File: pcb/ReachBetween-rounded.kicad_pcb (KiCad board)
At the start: 2 copper layers, 51.8 x 73.5 mm, 11 parts, among them J1 IN, J2 Out A, J3 Out B

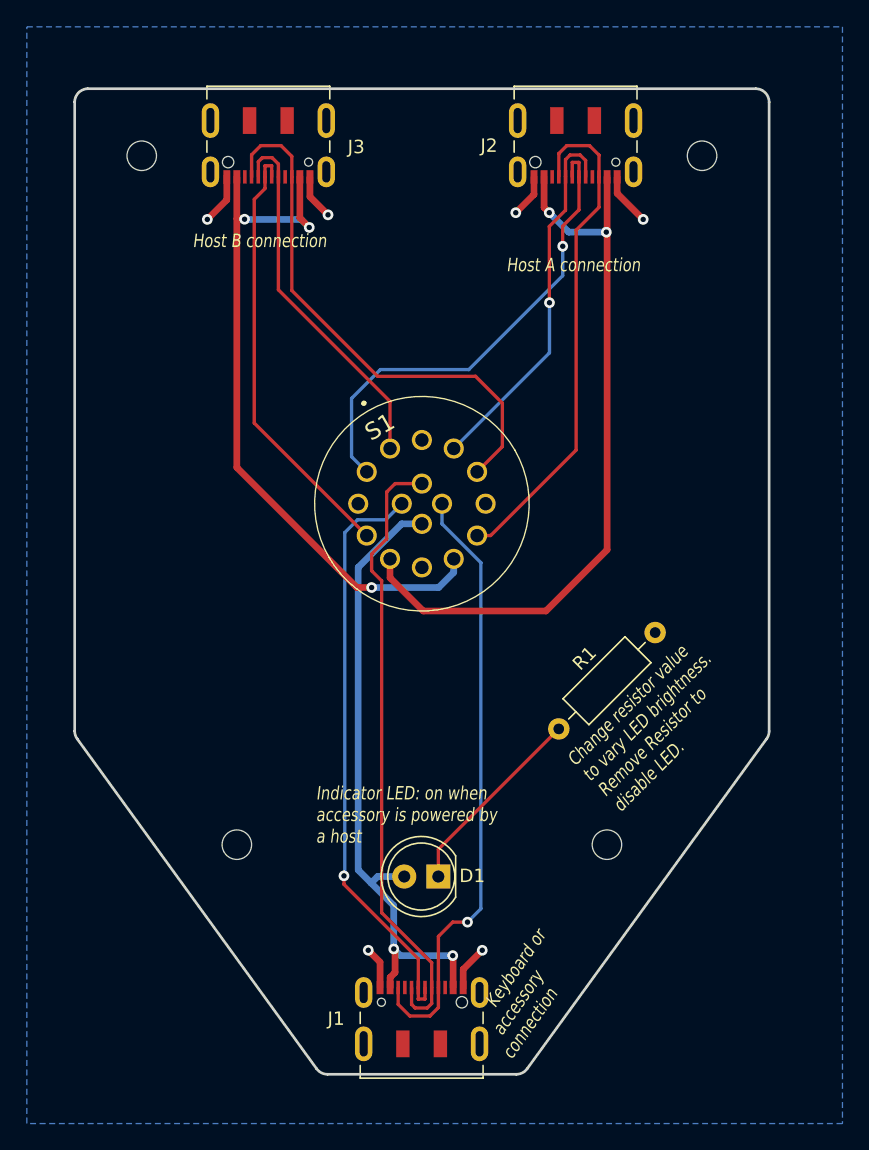
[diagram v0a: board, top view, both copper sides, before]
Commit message: Round tracks
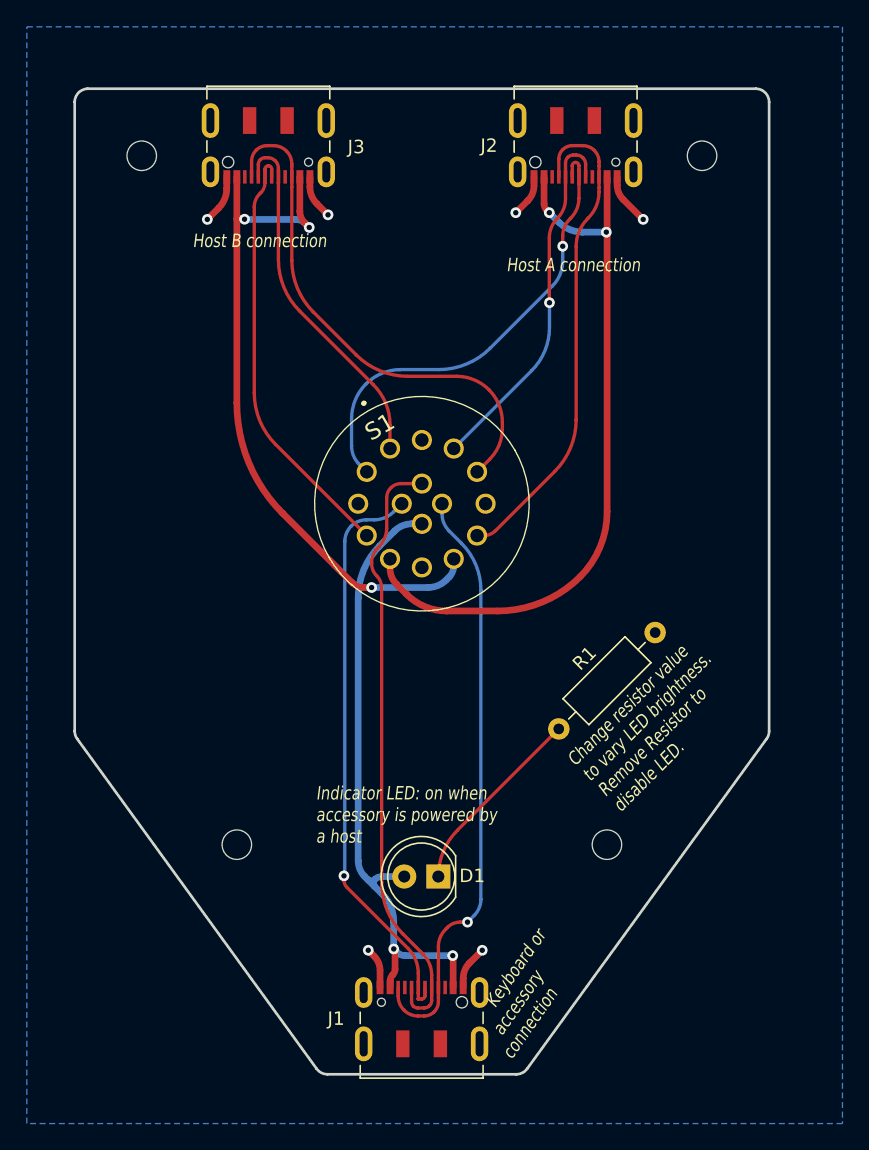
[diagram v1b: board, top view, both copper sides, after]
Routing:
- net /D+ A: track 36.0 -> 34.8 mm
- net /CC B: track 40.3 -> 39.1 mm
- net /VBUS A: track 56.0 -> 54.8 mm
- net /VBUS B: track 52.8 -> 51.9 mm
- net /D- in: track 46.4 -> 45.5 mm
- net /CC A: track 38.0 -> 37.2 mm
- net /CC in: track 45.6 -> 44.8 mm
- net /D+ B: track 32.7 -> 32.1 mm
- net /D- B: track 27.6 -> 27.0 mm
- net /D- A: track 28.0 -> 27.5 mm
- net /D+ in: track 43.6 -> 43.1 mm

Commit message: Teardrop tracks
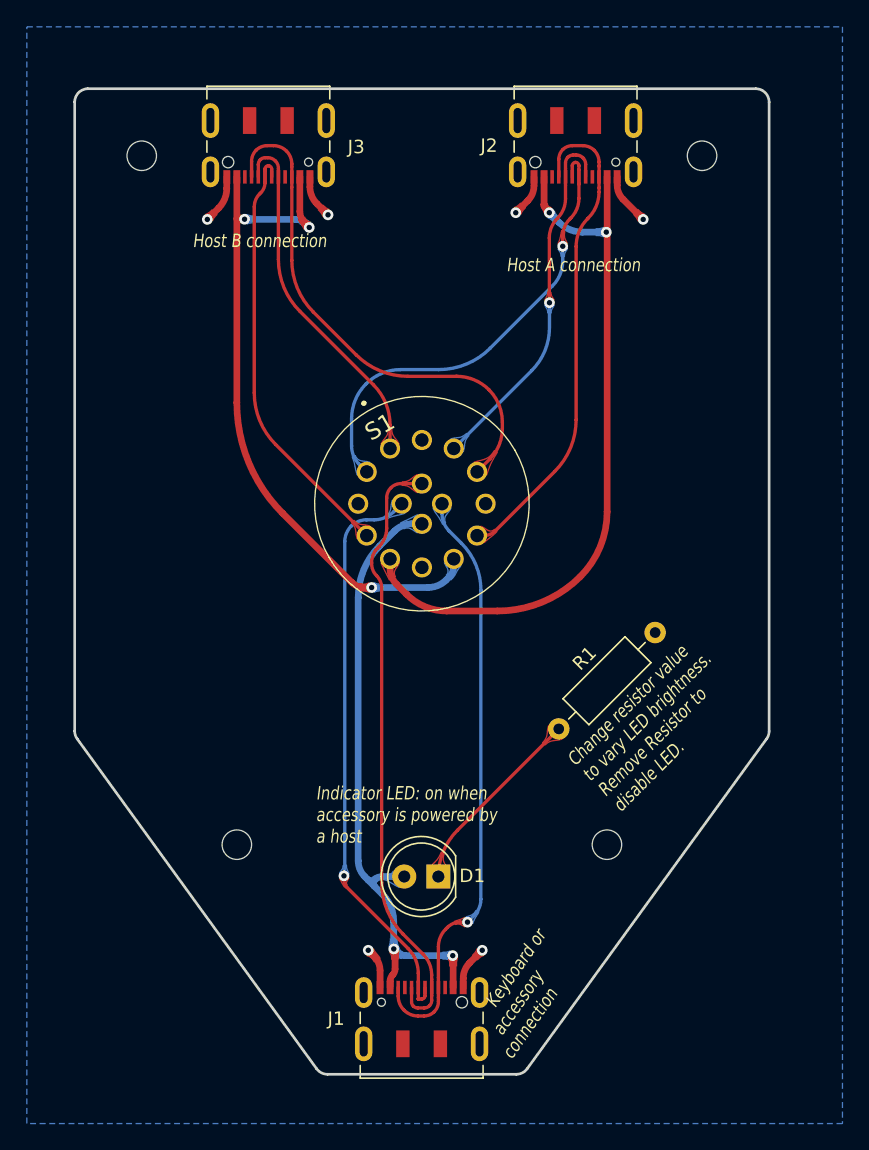
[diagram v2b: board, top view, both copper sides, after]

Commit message: Update version number
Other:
- board text added: "RB02 v1.1.2 © Will Harris-Braun 2022-04-17"
- board text removed: "RB02 v1.1.0 © Will Harris-Braun 2022-04-17"
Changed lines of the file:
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@@
     (effects (font (size 1.5 1.3) (thickness 0.3)) (justify mirror))
   )
-  (gr_text "RB02 v1.1.0\n© Will Harris-Braun\n2022-04-17" (at 142.5 94.2) (layer "B.SilkS")
+  (gr_text "RB02 v1.1.2\n© Will Harris-Braun\n2022-04-17" (at 142.5 94.2) (layer "B.SilkS")
     (effects (font (size 1 0.8) (thickness 0.1)) (justify left mirror))
   )

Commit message: Round silkscreen lines on back
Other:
- board text added: "RB02 v1.1.3 © Will Harris-Braun 2022-04-17"
- board text removed: "RB02 v1.1.2 © Will Harris-Braun 2022-04-17"
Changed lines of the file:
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@@
     ) (layer "B.SilkS") (width 0.025) (fill solid))
   (gr_rect (start 151 117.7) (end 149 119.7) (layer "B.SilkS") (width 0) (fill solid))
-  (gr_line (start 143.75 89.7) (end 138.5 85.7) (layer "B.SilkS") (width 2))
   (gr_poly
     (pts
@@
   (gr_rect (start 149 126.2) (end 151 124.2) (layer "B.SilkS") (width 0) (fill solid))
   (gr_line (start 150 101.8) (end 150 118.7) (layer "B.SilkS") (width 2))
+  (gr_arc (start 161.6 80.9) (mid 160.542149 85.3677) (end 157.55 88.85) (layer "B.SilkS") (width 2))
+  (gr_poly
+    (pts
+      (xy 143.401315 88.331702)
+      (xy 144.962176 89.582187)
+      (xy 143.711691 91.143048)
+      (xy 142.15083 89.892563)
+    ) (layer "B.SilkS") (width 0) (fill solid))
+  (gr_line (start 143.5 89.7) (end 142.45 88.85) (layer "B.SilkS") (width 2))
   (gr_rect (start 149 102.7) (end 151 100.7) (layer "B.SilkS") (width 0) (fill solid))
-  (gr_line (start 161.5 85.7) (end 161.5 69.25) (layer "B.SilkS") (width 2))
+  (gr_line (start 161.6 80.9) (end 161.5 69.25) (layer "B.SilkS") (width 2))
   (gr_poly
     (pts
@@
       (xy 139.95605 109.05397)
     ) (layer "B.SilkS") (width 0.025) (fill solid))
-  (gr_line (start 161.5 85.7) (end 156.5 89.7) (layer "B.SilkS") (width 2))
-  (gr_line (start 138.5 85.25) (end 138.5 69.25) (layer "B.SilkS") (width 2))
+  (gr_line (start 157.55 88.85) (end 156.5 89.7) (layer "B.SilkS") (width 2))
+  (gr_arc (start 142.45 88.85) (mid 139.457837 85.367706) (end 138.4 80.9) (layer "B.SilkS") (width 2))
   (gr_poly
     (pts
@@
       (xy 137.557997 109.051969)
     ) (layer "B.SilkS") (width 0.025) (fill solid))
+  (gr_line (start 138.5 69.25) (end 138.4 80.9) (layer "B.SilkS") (width 2))
   (gr_poly
     (pts
@@
   (gr_poly
     (pts
-      (xy 145.157798 89.511062)
-      (xy 143.566851 88.299085)
-      (xy 142.354874 89.890032)
-      (xy 143.945821 91.102009)
-    ) (layer "B.SilkS") (width 0) (fill solid))
-  (gr_poly
-    (pts
       (xy 156.598685 88.331702)
       (xy 155.037824 89.582187)
@@
     (effects (font (size 1.5 1.3) (thickness 0.3)) (justify mirror))
   )
-  (gr_text "RB02 v1.1.2\n© Will Harris-Braun\n2022-04-17" (at 142.5 94.2) (layer "B.SilkS")
+  (gr_text "RB02 v1.1.3\n© Will Harris-Braun\n2022-04-17" (at 142.5 94.2) (layer "B.SilkS")
     (effects (font (size 1 0.8) (thickness 0.1)) (justify left mirror))
   )
